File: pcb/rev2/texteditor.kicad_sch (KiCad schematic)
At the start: 17 parts, among them J2 LCD IDC, J3 Power In (7v-20v), J4 LED, J5 Contrast Pot, J6 Brightness Pot, J7 SD_Card_Receptacle, Q1 BC547, SW1 Input Type Switch, SW2 Power Switch, U1 L7805

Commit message: switch towurth socket
need to reroute some stuff now
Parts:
- added J1: Unsaved Changes LED, Connector_JST:JST_XA_B02B-XASK-1_1x02_P2.50mm_Vertical, symbol Connector_Generic:Conn_01x02
- added R3: 220Ω, Resistor_THT:R_Axial_DIN0207_L6.3mm_D2.5mm_P10.16mm_Horizontal, symbol Device:R
- J7: footprint Connector_Card:SD_TE_2041021 -> wurth:693063010911
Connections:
- net +5V: no longer Q1.1 (C)
- net GND: now also J1.2 (Pin_2); no longer J4.2 (Pin_2)
- net at A1.6 (GPIO4): now also R3.2
- new net: J1.1 (Pin_1), R3.1
- new net: J4.2 (Pin_2), Q1.1 (C)
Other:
- moved on the sheet: J4

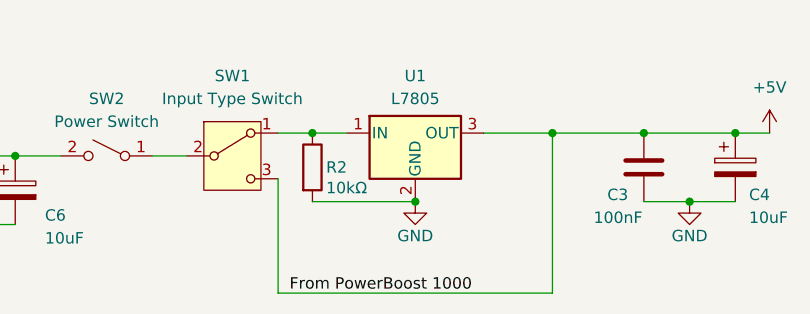
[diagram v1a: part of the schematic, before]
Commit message: Re-routed new socket footprint
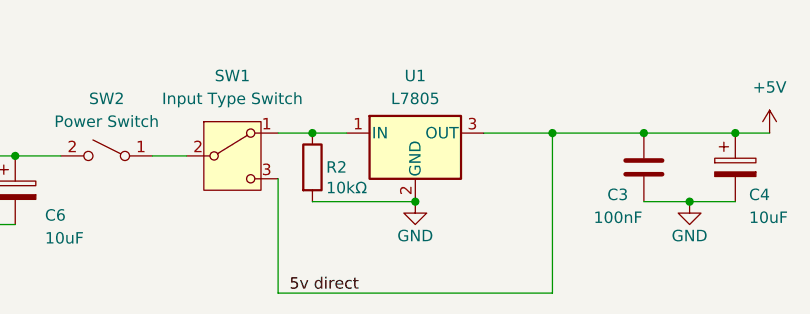
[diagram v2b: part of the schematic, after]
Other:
- title: (none) -> Codex
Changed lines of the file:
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@@
 	(generator_version "10.0")
 	(paper "A4")
+	(title_block
+		(title "Codex")
+		(date "2026-06-24")
+		(rev "2")
+	)
 	(junction
 		(at 165.1 137.16)
@@
 		)
 	)
-	(label "From PowerBoost 1000"
+	(label "5v direct"
 		(at 135.89 154.94 0)
 		(effects

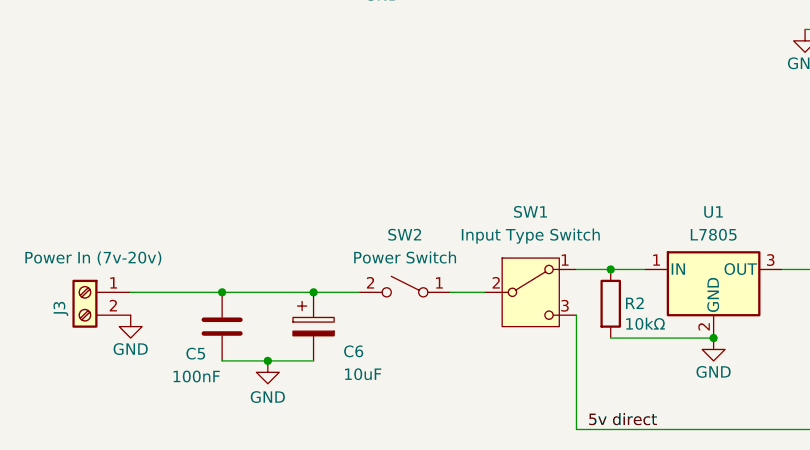
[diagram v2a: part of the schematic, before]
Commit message: add some extra silkscreen to pcb
flip a symbol on the schematic so routing is less dumb
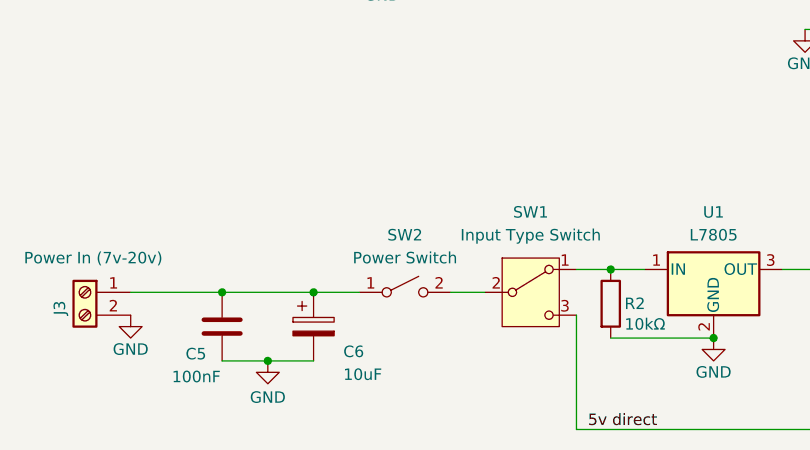
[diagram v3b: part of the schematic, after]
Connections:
- net at C5.1, C6.1, J3.1 (Pin_1): now also SW2.1 (A); no longer SW2.2 (B)
- net at SW1.2 (B): now also SW2.2 (B); no longer SW2.1 (A)
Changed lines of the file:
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@@
 		(lib_id "Switch:SW_SPST")
 		(at 115.57 139.7 0)
-		(mirror y)
 		(unit 1)
 		(body_style 1)

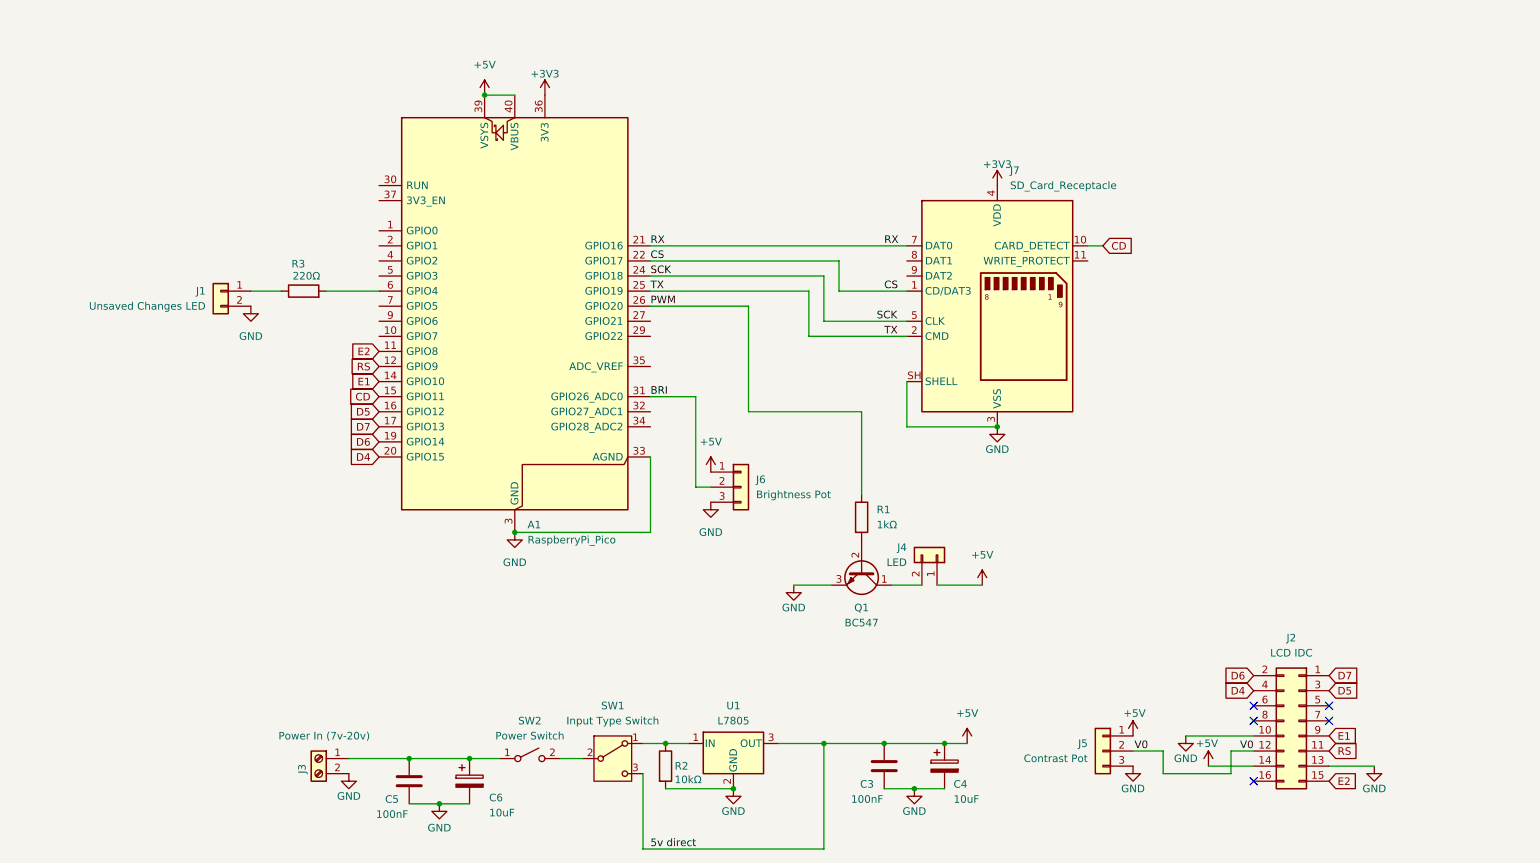
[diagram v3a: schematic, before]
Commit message: Some board and schematic adjustments
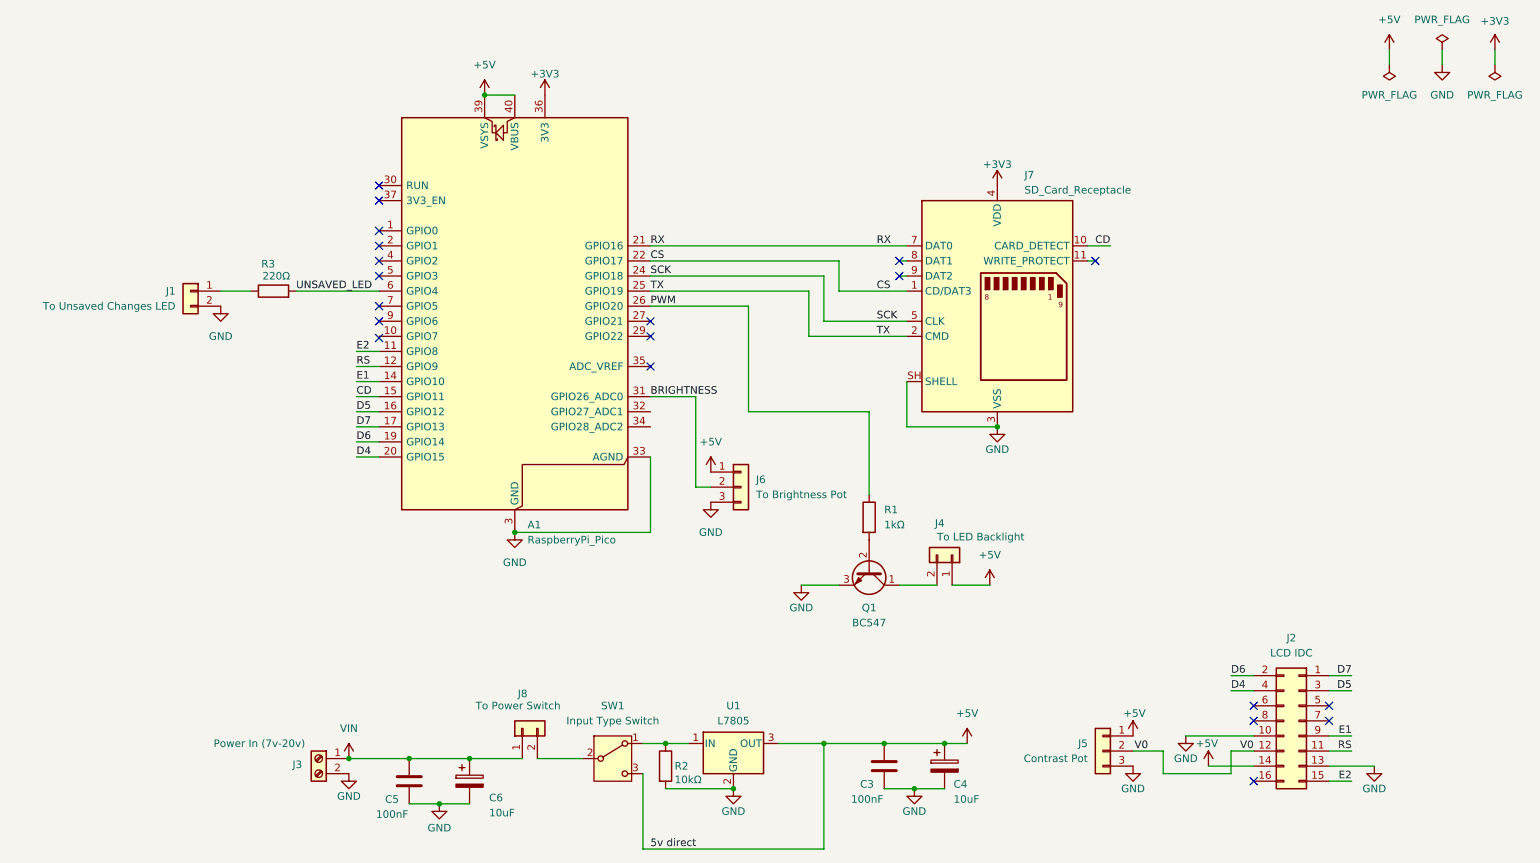
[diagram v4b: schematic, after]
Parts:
- removed SW2: Power Switch, Connector_JST:JST_XA_B02B-XASK-1_1x02_P2.50mm_Vertical, symbol Switch:SW_SPST
- added J8: To Power Switch, Connector_JST:JST_XA_B02B-XASK-1_1x02_P2.50mm_Vertical, symbol Connector_Generic:Conn_01x02
- J1: value Unsaved Changes LED -> To Unsaved Changes LED
- J4: value LED -> To LED Backlight
- J6: value Brightness Pot -> To Brightness Pot
- SW1: footprint Connector_PinHeader_2.54mm:PinHeader_1x03_P2.54mm_Vertical -> SLW_883935_2A_D:SW_SLW-883935-2A-D
- U1: footprint Connector_PinSocket_2.54mm:PinSocket_1x03_P2.54mm_Vertical -> Package_TO_SOT_THT:TO-220-3_Vertical
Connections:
- net VIN: now reaches C5.1, C6.1, J3.1 (Pin_1)
- net VIN: now also J8.1 (Pin_1)
- net at SW1.2 (B): now also J8.2 (Pin_2)
- net UNSAVED_LED: now reaches A1.6 (GPIO4), R3.2
- net BRI renamed BRIGHTNESS
- no-connect marks 5 -> 20
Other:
- moved on the sheet: J1, J4, Q1, R1, R3
